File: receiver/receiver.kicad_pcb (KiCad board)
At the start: 2 copper layers, 58.7 x 53.8 mm, 62 parts, among them J1 USB_B_Mini, J2 Conn_01x04_Pin, J3 Conn_01x04_Pin, SW1 SW_Push, SW2 SW_SPDT, U1 AMS1117-3.3, U2 STM32F303K8Tx, U3 Si590, U4 HMC356, U5 LT5517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

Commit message: Finished PCB design
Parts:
- removed U8: AMK-2-13+, Communication_circuit:6-SMD-2.54
- added AE1: Antenna_Shield, Connector_Coaxial:U.FL_Molex_MCRF_73412-0110_Vertical, F.Cu at (107.2, 118.9)
- added C13: 220p, Capacitor_SMD:C_0603_1608Metric_Pad1.08x0.95mm_HandSolder, F.Cu at (108.8, 103.5)
- added C16: 220p, Capacitor_SMD:C_0603_1608Metric_Pad1.08x0.95mm_HandSolder, F.Cu at (108.8, 105.2)
- added H1: MountingHole_Pad, MountingHole:MountingHole_2.2mm_M2_DIN965_Pad, F.Cu at (85.5, 73.5)
- added H2: MountingHole_Pad, MountingHole:MountingHole_2.2mm_M2_DIN965_Pad, F.Cu at (133.5, 73.5)
- added H3: MountingHole_Pad, MountingHole:MountingHole_2.2mm_M2_DIN965_Pad, F.Cu at (133.5, 122.5)
- added H4: MountingHole_Pad, MountingHole:MountingHole_2.2mm_M2_DIN965_Pad, F.Cu at (85.5, 122.5)
- added R2: 1.5k, Resistor_SMD:R_0603_1608Metric_Pad0.98x0.95mm_HandSolder, F.Cu at (124.0, 79.4)
- added R6: 3.9k, Resistor_SMD:R_0603_1608Metric_Pad0.98x0.95mm_HandSolder, F.Cu at (119.7, 123.8)
- added RV1: R_Potentiometer, Potentiometer_SMD:Potentiometer_ACP_CA6-VSMD_Vertical, F.Cu at (123.9, 118.5)
- U3: value Si590 -> MAX2622; footprint Oscillator:Oscillator_SMD_IDT_JU6-6_7.0x5.0mm_P2.54mm -> Package_SO:TSSOP-8_4.4x3mm_P0.65mm
- moved C37 21.7 mm to (113.3, 81.4), turned to -90 degrees
- moved C10 19.3 mm to (125.6, 101.6), turned to 180 degrees
- moved D1 18.8 mm to (129.8, 99.2), turned to 180 degrees
- moved C35 18.6 mm to (96.9, 123.1)
- moved L6 18.6 mm to (103.2, 118.1)
- moved L7 18.6 mm to (99.0, 123.1)
- moved U4 18.6 mm to (98.7, 119.1)
- moved C34 18.1 mm to (99.5, 116.0)
- moved C36 18.1 mm to (112.2, 84.5), turned to 0 degrees
- moved C2 16.5 mm to (94.6, 119.4)
- moved C38 16.2 mm to (112.2, 86.1), turned to 0 degrees
- moved R3 16.0 mm to (132.9, 100.1), turned to -90 degrees
- moved C7 15.6 mm to (88.7, 117.8)
- moved L1 15.6 mm to (91.6, 116.9)
- moved C4 15.3 mm to (93.7, 116.9)
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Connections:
- net RF_ANTENNA_INPUT renamed Net-(AE1-A)
- C37 pad 2: +3V3 -> 3V3
- J2 pad 2: USART1_RX -> USART1_TX
- J2 pad 3: USART1_TX -> USART1_RX
- J3 pad 2: SWDIO -> SWCLK
- J3 pad 3: SWCLK -> SWDIO
- R13 pad 1: +5V -> +3V3
- R14 pad 1: +5V -> +3V3
- U2 pad 21: USART1_CTS -> unconnected-(U2-PA11-Pad21)
- U2 pad 22: USART1_RTS -> unconnected-(U2-PA12-Pad22)
- U3 pad 1: +3V3 -> unconnected-(U3-NC-Pad1)
- U3 pad 2: unconnected-(U3-OC-Pad2) -> Net-(U3-TUNE)
- U3 pad 4: Net-(U3-CLK_P) -> +3V3
- U3 pad 5: unconnected-(U3-CLK_N-Pad5) -> +3V3
- U7 pad 11: USART1_RTS -> unconnected-(U7-CTS-Pad11)
- U7 pad 17: +3V3 -> 3V3
- U7 pad 3: USART1_CTS -> unconnected-(U7-RTS-Pad3)
- U7 pad 4: +3V3 -> 3V3
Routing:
- net +3V3: track 11.2 -> 147.9 mm, vias 0 -> 2
- net +5V: track 19.1 -> 118.3 mm, vias 0 -> 2
- net 3V3: track 0.00 -> 39.6 mm
- net EN: track 2.08 -> 34.6 mm, vias 0 -> 2
- net GND: track 0.00 -> 29.3 mm, vias 0 -> 37
- net USART1_RTS: track 20.0 -> 0.00 mm
- net USART1_CTS: track 14.3 -> 0.00 mm
- net TX_LED: track 4.51 -> 16.9 mm, vias 0 -> 2
- net USB_D+: track 7.02 -> 18.7 mm
- net USB_D-: track 8.08 -> 18.7 mm
- net RX_LED: track 2.71 -> 12.2 mm, vias 0 -> 2
- net Net-(D2-A): track 1.85 -> 6.85 mm
- net BPF_output: track 8.59 -> 3.91 mm
- net USART1_RX: track 29.3 -> 33.8 mm
- net Net-(U3-CLK_P): track 4.33 -> 0.00 mm
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- added copper zone on B.Cu, net GND
- added copper zone on F.Cu, net GND
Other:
- board size 58.7 x 53.8 mm -> 55 x 56 mm
- board text added: "SWD"
- board text added: "UART"

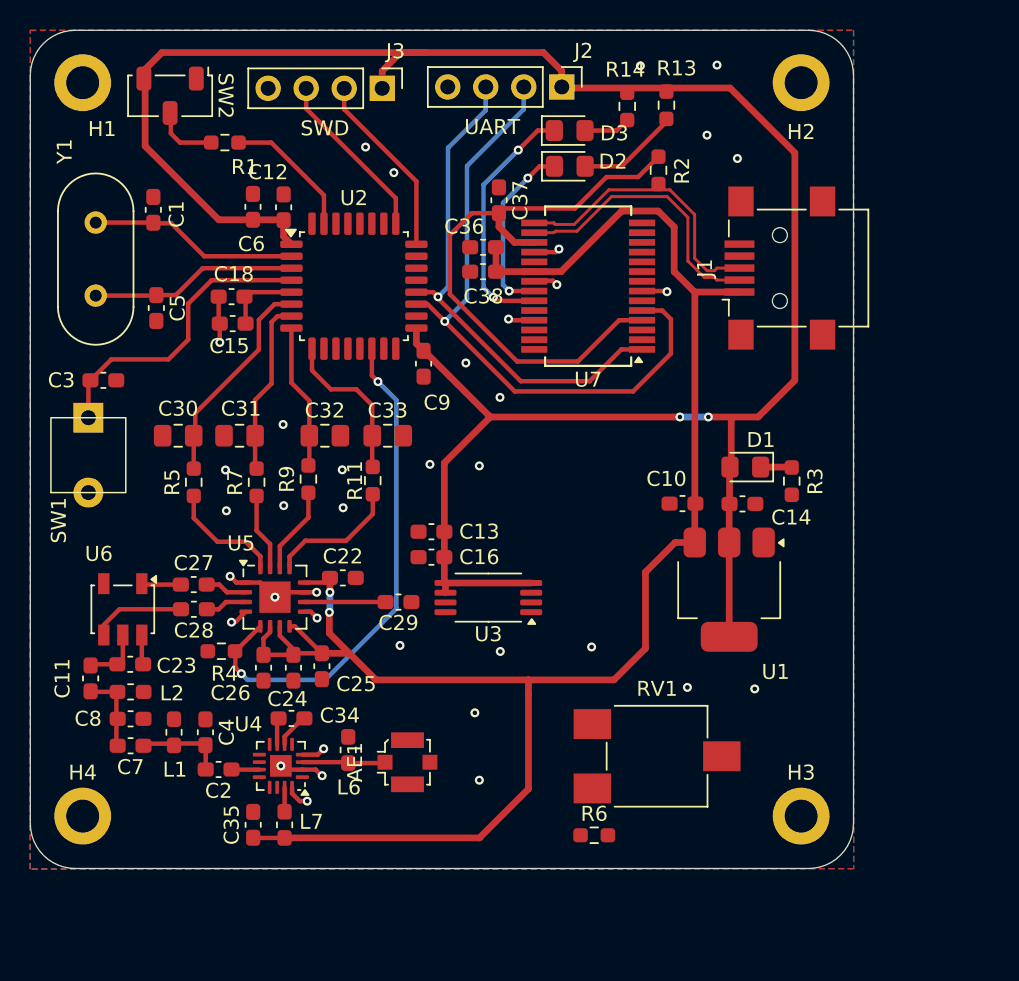
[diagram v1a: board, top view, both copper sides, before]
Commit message: First design of sended PCBs
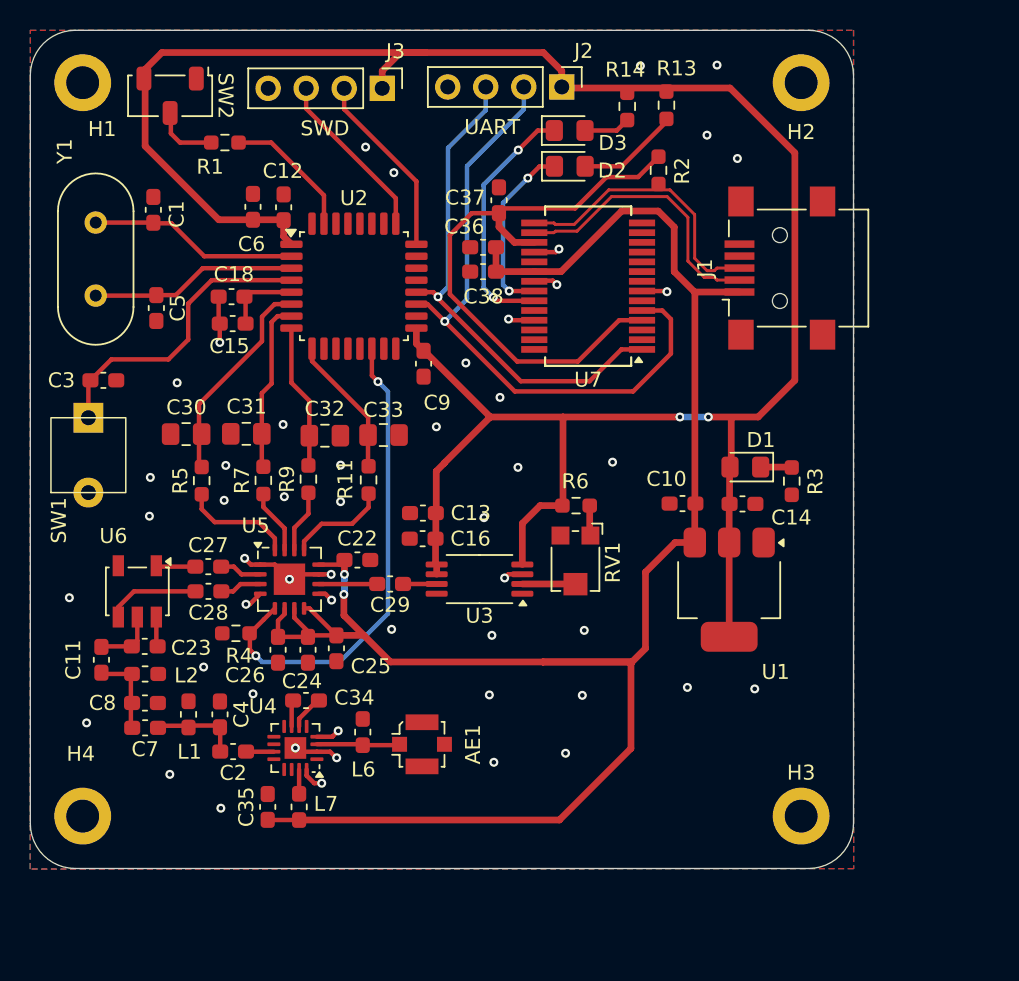
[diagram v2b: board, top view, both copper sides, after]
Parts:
- RV1: footprint Potentiometer_SMD:Potentiometer_ACP_CA6-VSMD_Vertical -> Potentiometer_SMD:Potentiometer_Bourns_TC33X_Vertical
- moved R6 22.1 mm to (118.5, 101.8), turned to 180 degrees
- moved RV1 14.0 mm to (118.4, 105.6), turned to -90 degrees
- moved AE1 1.54 mm to (108.2, 117.7)
- moved C2 1.54 mm to (95.5, 118.2)
- moved C23 1.54 mm to (89.6, 111.2)
- moved C25 1.54 mm to (102.5, 111.3)
- moved C27 1.54 mm to (93.9, 105.8)
- moved C28 1.54 mm to (93.9, 107.5)
- moved C4 1.54 mm to (94.7, 115.7)
- moved L1 1.54 mm to (92.6, 115.7)
- moved L2 1.54 mm to (89.7, 113.0)
- moved R4 1.54 mm to (95.7, 110.3)
- moved U5 1.54 mm to (99.3, 106.7)
- moved U6 1.54 mm to (89.2, 107.5)
- moved C22 1.54 mm to (103.8, 105.4)
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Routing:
- net +5V: track 118.3 -> 127.8 mm
- net +3V3: track 147.9 -> 153.2 mm
- net Net-(U3-TUNE): track 0.00 -> 3.55 mm
- net LO_OUT: track 0.00 -> 2.25 mm
- net Q_OUT_N: track 8.82 -> 6.75 mm
- net EN: track 34.6 -> 32.5 mm
- net Net-(R6-Pad1): track 0.00 -> 2.02 mm
- net Q_OUT_P: track 5.81 -> 4.21 mm
- net Net-(U5-2XLO): track 5.44 -> 3.92 mm
- net GND: track 29.3 -> 30.6 mm, vias 37 -> 51
- net ADC1_IN4: track 10.6 -> 9.50 mm
- net I_OUT_N: track 5.19 -> 4.33 mm
- net BPF_output: track 3.91 -> 4.60 mm
